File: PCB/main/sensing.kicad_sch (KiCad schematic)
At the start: 0 parts

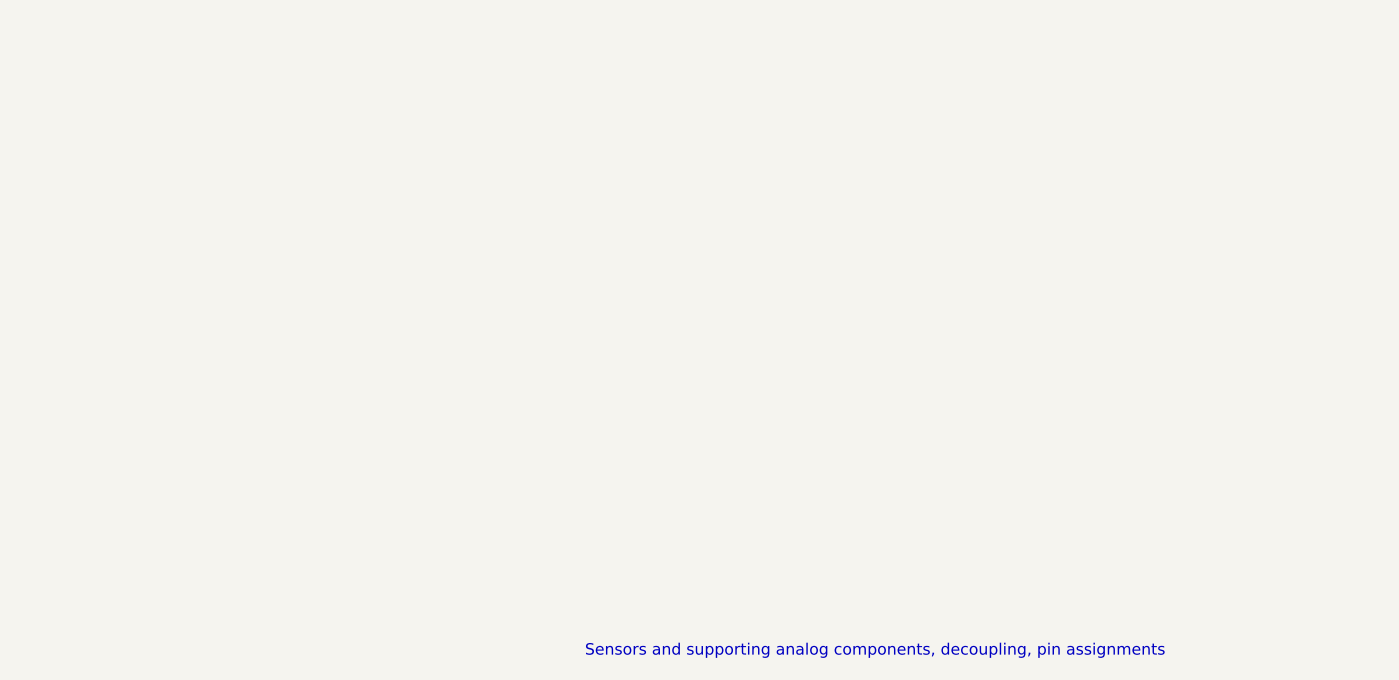
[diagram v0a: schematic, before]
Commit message: added digital sensors
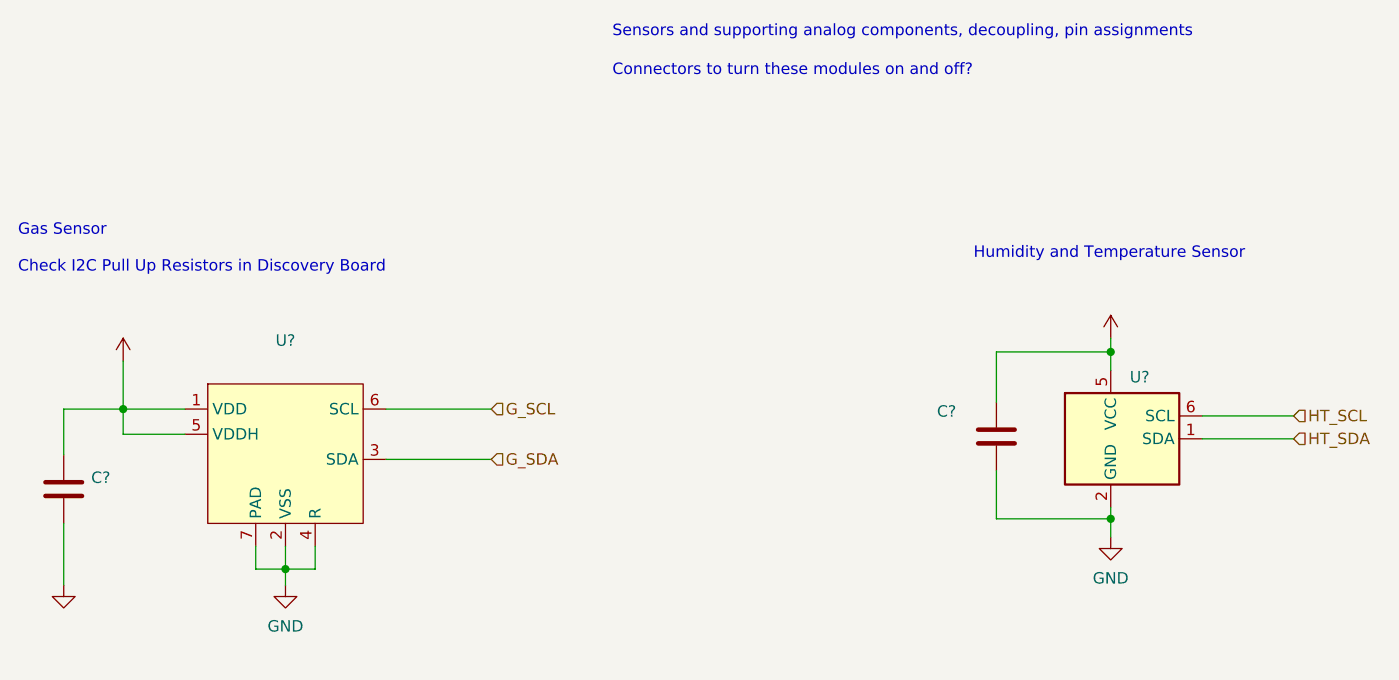
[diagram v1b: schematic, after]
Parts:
- added C? (x2): (no value), symbol Device:C
- added U?: (no value), symbol Sensor_Humidity:HDC1080
- added U?: (no value), symbol DiscoverAir:SGP30-2.5k
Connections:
- new net +1V8: C?.1, U?.1 (VDD), U?.5 (VDDH)
- new net +3V3: C?.1, U?.5 (VCC)
- new net GND: C?.2, C?.2, U?.2 (GND), U?.2 (VSS), U?.4 (R), U?.7 (PAD)
- new net G_SCL: U?.6 (SCL)
- new net G_SDA: U?.3 (SDA)
- new net HT_SCL: U?.6 (SCL)
- new net HT_SDA: U?.1 (SDA)
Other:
- note added: "Connectors to turn these modules on and off?"
- note added: "Gas Sensor Check I2C Pull Up Resistors in Discovery Board"
- note added: "Humidity and Temperature Sensor"
- company: (none) -> University of Cape Town
- title: (none) -> DiscoverAir HAT
